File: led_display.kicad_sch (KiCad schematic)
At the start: 192 parts, among them J6 Conn_02x07_Odd_Even

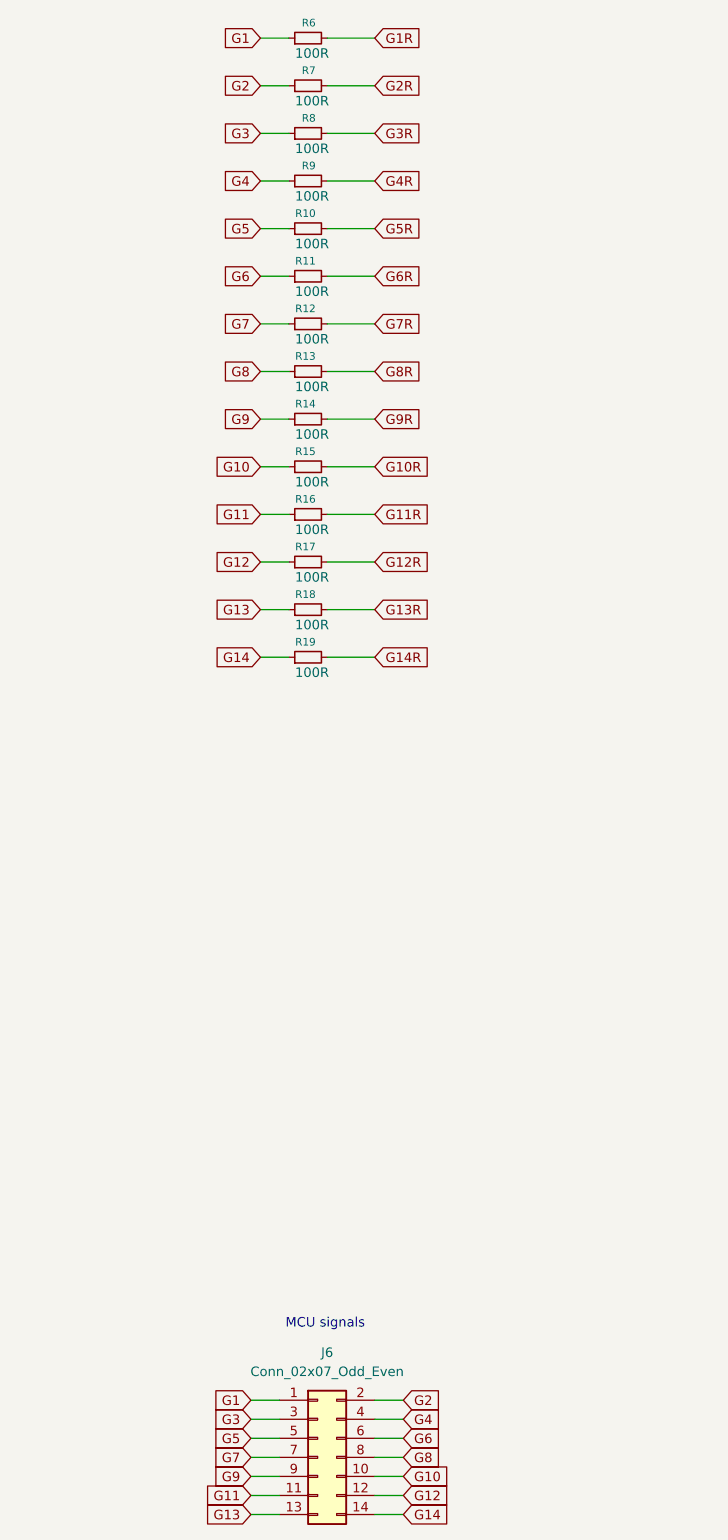
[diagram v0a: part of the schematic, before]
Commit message: Change of concept - one board, not multiple
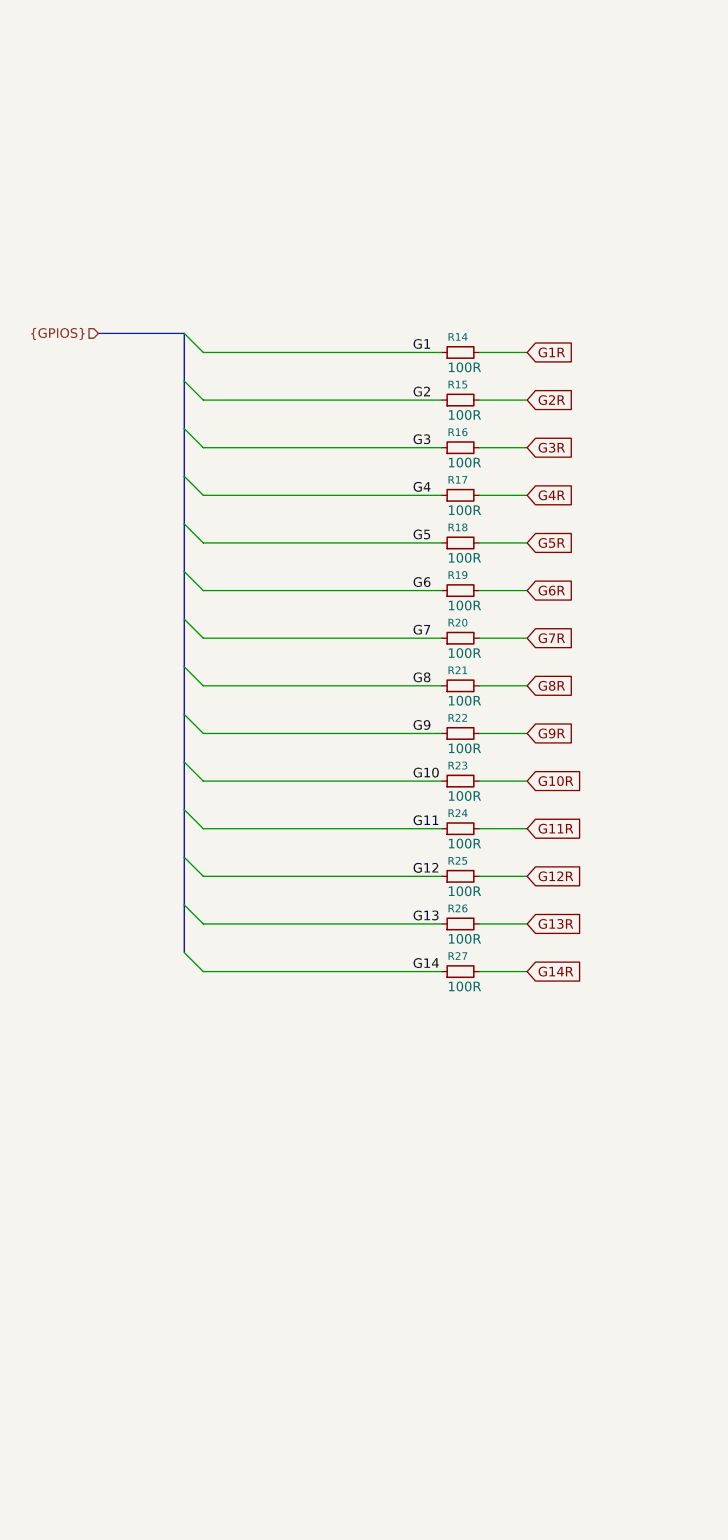
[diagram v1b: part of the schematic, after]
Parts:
- removed J6: Conn_02x07_Odd_Even, Connector_PinHeader_2.54mm:PinHeader_2x07_P2.54mm_Vertical, symbol Connector_Generic:Conn_02x07_Odd_Even
- renumbered R6 to R14, R7 to R15, R8 to R16, R9 to R17, R10 to R18, R11 to R19, R12 to R20, R13 to R21, R14 to R22, R15 to R23, R16 to R24, R17 to R25, R18 to R26, R19 to R27
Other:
- note removed: "MCU signals"
- moved on the sheet: R14, R15, R16, R17, R18, R19, R20, R21, R22, R23, R24, R25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

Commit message: Early pcb project
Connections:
- net G10R: now also D114.1 (K)
- net G11R: now also D115.1 (K)
- net G12R: now also D116.1 (K)
- net G13R: now also D117.1 (K)
- net G14R: now also D118.1 (K)
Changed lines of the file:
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@@
 	(global_label "G11R"
 		(shape input)
-		(at 232.41 153.67 270)
+		(at 233.68 153.67 270)
 		(fields_autoplaced yes)
 		(effects
@@
 		)
 		(property "Intersheetrefs" "${INTERSHEET_REFS}"
-			(at 232.41 161.6142 90)
+			(at 233.68 161.6142 90)
 			(effects
 				(font
@@
 	(global_label "G12R"
 		(shape input)
-		(at 245.11 153.67 270)
+		(at 246.38 153.67 270)
 		(fields_autoplaced yes)
 		(effects
@@
 		)
 		(property "Intersheetrefs" "${INTERSHEET_REFS}"
-			(at 245.11 161.6142 90)
+			(at 246.38 161.6142 90)
 			(effects
 				(font
@@
 	(global_label "G14R"
 		(shape input)
-		(at 270.51 153.67 270)
+		(at 271.78 153.67 270)
 		(fields_autoplaced yes)
 		(effects
@@
 		)
 		(property "Intersheetrefs" "${INTERSHEET_REFS}"
-			(at 270.51 161.6142 90)
+			(at 271.78 161.6142 90)
 			(effects
 				(font
@@
 	(global_label "G13R"
 		(shape input)
-		(at 257.81 153.67 270)
+		(at 259.08 153.67 270)
 		(fields_autoplaced yes)
 		(effects
@@
 		)
 		(property "Intersheetrefs" "${INTERSHEET_REFS}"
-			(at 257.81 161.6142 90)
+			(at 259.08 161.6142 90)
 			(effects
 				(font
@@
 	(global_label "G10R"
 		(shape input)
-		(at 219.71 153.67 270)
+		(at 220.98 153.67 270)
 		(fields_autoplaced yes)
 		(effects
@@
 		)
 		(property "Intersheetrefs" "${INTERSHEET_REFS}"
-			(at 219.71 161.6142 90)
+			(at 220.98 161.6142 90)
 			(effects
 				(font

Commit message: Finished pcb project
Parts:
- renumbered D69 to D10, D22 to D100, D34 to D101, D47 to D102, D61 to D103, D76 to D104, D91 to D105, D121 to D107, D135 to D108, D148 to D109, D84 to D11, D160 to D110, D170 to D111, D177 to D112, D6 to D113, D13 to D114, D23 to D115, D35 to D116, D48 to D117, D62 to D118, D77 to D119, D99 to D12, D92 to D120, D107 to D121, D136 to D123, D149 to D124, D161 to D125, D171 to D126, D178 to D127, D14 to D128, D24 to D129, D114 to D13, D36 to D130, D49 to D131, D63 to D132, D78 to D133, D93 to D134, D108 to D135, D123 to D136, D150 to D138, D162 to D139, D128 to D14, D172 to D140, D15 to D141, D25 to D142, D37 to D143, D50 to D144, D64 to D145, D79 to D146, D94 to D147, D109 to D148, D124 to D149, D141 to D15, D138 to D150, D163 to D152, D173 to D153, D26 to D154, D38 to D155, D51 to D156, D65 to D157, D80 to D158, D95 to D159, D110 to D160, D125 to D161, D139 to D162, D152 to D163, D39 to D165, D52 to D166, D66 to D167, D81 to D168, D96 to D169, D28 to D17, D111 to D170, D126 to D171, D140 to D172, D153 to D173, D67 to D174, D82 to D175, D97 to D176, D112 to D177, D127 to D178, D41 to D18, D55 to D19, D53 to D2, D70 to D20, D85 to D21, D100 to D22, D115 to D23, D129 to D24, D142 to D25, D154 to D26, D7 to D27, D17 to D28, D68 to D3, D42 to D30, D56 to D31, D71 to D32, D86 to D33, D101 to D34, D116 to D35, D130 to D36, D143 to D37, D155 to D38, D165 to D39, D83 to D4, D8 to D40, D18 to D41, D30 to D42, D57 to D44, D72 to D45, D87 to D46, D102 to D47, D117 to D48, D131 to D49, D98 to D5, D144 to D50, D156 to D51, D166 to D52, D2 to D53, D9 to D54, D19 to D55, D31 to D56, D44 to D57, D73 to D59, D113 to D6, D88 to D60, D103 to D61, D118 to D62, D132 to D63, D145 to D64, D157 to D65, D167 to D66, D174 to D67, D3 to D68, D10 to D69, D27 to D7, D20 to D70, D32 to D71, D45 to D72, D59 to D73, D89 to D75, D104 to D76, D119 to D77, D133 to D78, D146 to D79, D40 to D8, D158 to D80, D168 to D81, D175 to D82, D4 to D83, D11 to D84, D21 to D85, D33 to D86, D46 to D87, D60 to D88, D75 to D89, D54 to D9, D105 to D91, D120 to D92, D134 to D93, D147 to D94, D159 to D95, D169 to D96, D176 to D97, D5 to D98, D12 to D99, R17 to R10, R18 to R11, R19 to R12, R20 to R13, R21 to R14, R22 to R15, R23 to R16, R24 to R17, R25 to R18, R26 to R19, R27 to R20, R14 to R7, R15 to R8, R16 to R9
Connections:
- net G10R: now also D14.2 (A), D161.2 (A), D171.2 (A), D49.2 (A)

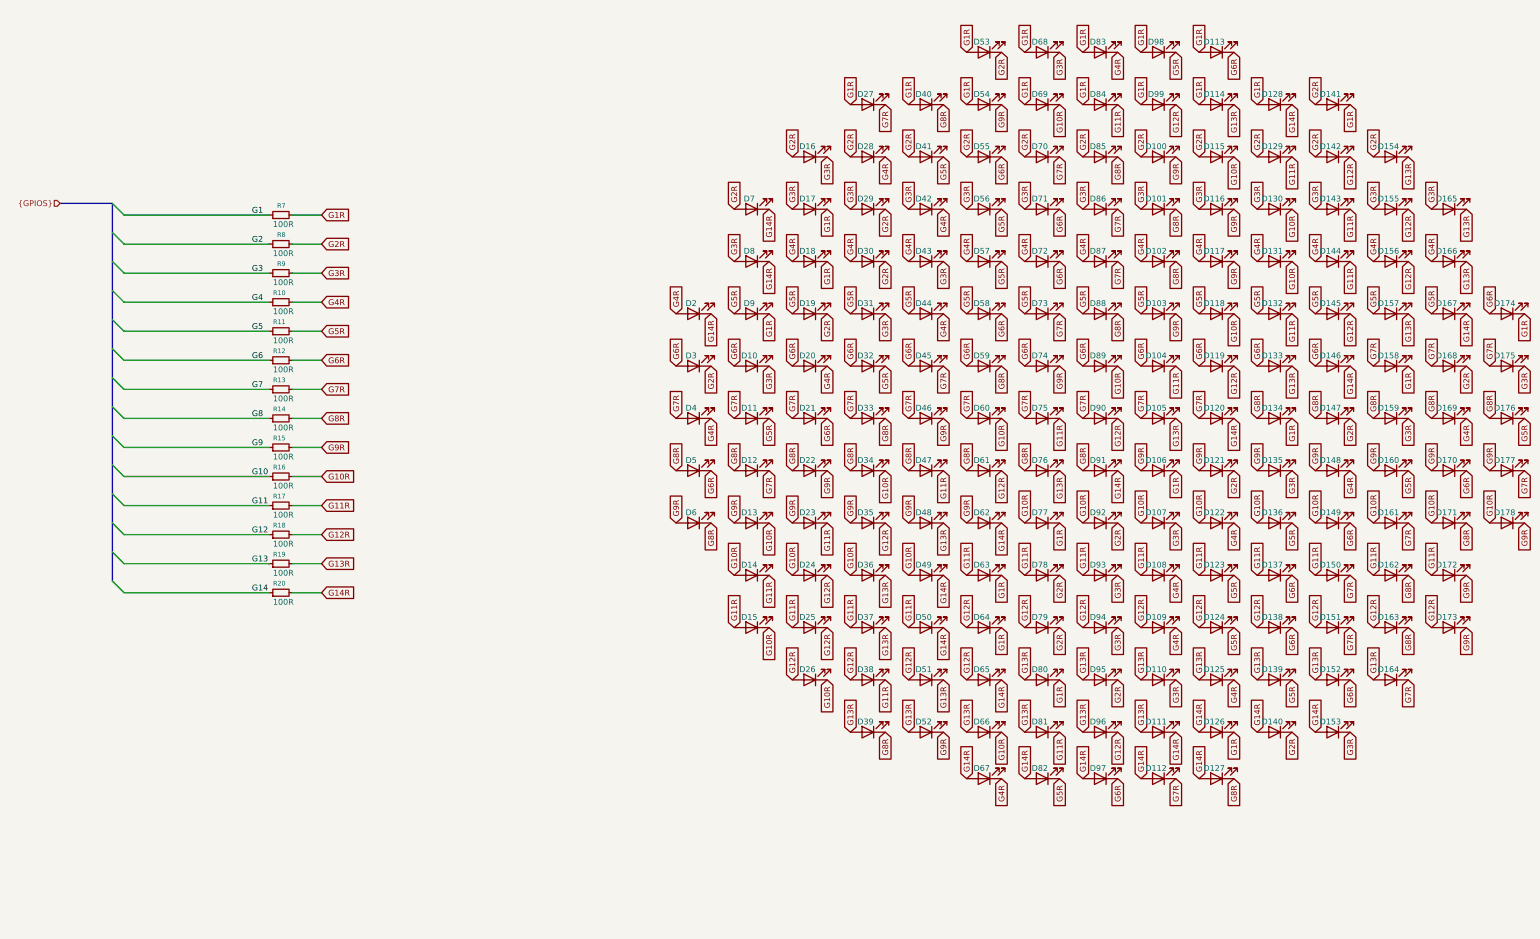
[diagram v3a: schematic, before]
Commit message: Add new mcu and better leds layout
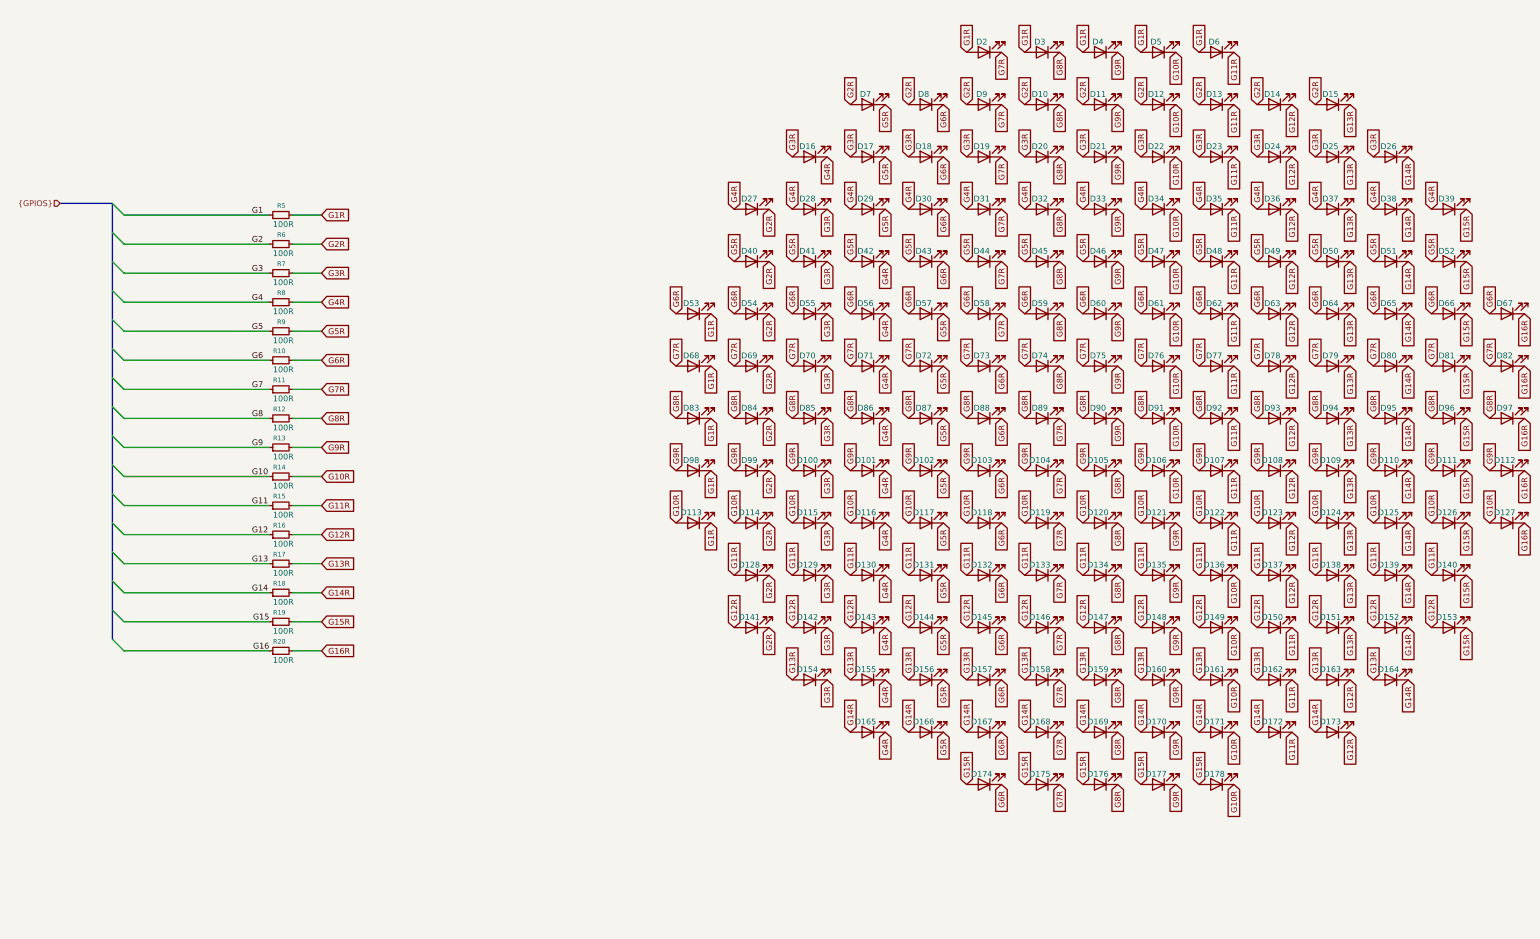
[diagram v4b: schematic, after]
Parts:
- added R19, R20: 100R, Resistor_SMD:R_0603_1608Metric, symbol Device:R_Small
- renumbered D69 to D10, D22 to D100, D34 to D101, D47 to D102, D61 to D103, D76 to D104, D91 to D105, D121 to D107, D135 to D108, D148 to D109, D84 to D11, D160 to D110, D170 to D111, D177 to D112, D6 to D113, D13 to D114, D23 to D115, D35 to D116, D48 to D117, D62 to D118, D77 to D119, D99 to D12, D92 to D120, D107 to D121, D136 to D123, D149 to D124, D161 to D125, D171 to D126, D178 to D127, D14 to D128, D24 to D129, D114 to D13, D36 to D130, D49 to D131, D63 to D132, D78 to D133, D93 to D134, D108 to D135, D123 to D136, D150 to D138, D162 to D139, D128 to D14, D172 to D140, D15 to D141, D25 to D142, D37 to D143, D50 to D144, D64 to D145, D79 to D146, D94 to D147, D109 to D148, D124 to D149, D141 to D15, D138 to D150, D163 to D152, D173 to D153, D26 to D154, D38 to D155, D51 to D156, D65 to D157, D80 to D158, D95 to D159, D110 to D160, D125 to D161, D139 to D162, D152 to D163, D39 to D165, D52 to D166, D66 to D167, D81 to D168, D96 to D169, D28 to D17, D111 to D170, D126 to D171, D140 to D172, D153 to D173, D67 to D174, D82 to D175, D97 to D176, D112 to D177, D127 to D178, D41 to D18, D55 to D19, D53 to D2, D70 to D20, D85 to D21, D100 to D22, D115 to D23, D129 to D24, D142 to D25, D154 to D26, D7 to D27, D17 to D28, D68 to D3, D42 to D30, D56 to D31, D71 to D32, D86 to D33, D101 to D34, D116 to D35, D130 to D36, D143 to D37, D155 to D38, D165 to D39, D83 to D4, D8 to D40, D18 to D41, D30 to D42, D57 to D44, D72 to D45, D87 to D46, D102 to D47, D117 to D48, D131 to D49, D98 to D5, D144 to D50, D156 to D51, D166 to D52, D2 to D53, D9 to D54, D19 to D55, D31 to D56, D44 to D57, D73 to D59, D113 to D6, D88 to D60, D103 to D61, D118 to D62, D132 to D63, D145 to D64, D157 to D65, D167 to D66, D174 to D67, D3 to D68, D10 to D69, D27 to D7, D20 to D70, D32 to D71, D45 to D72, D59 to D73, D89 to D75, D104 to D76, D119 to D77, D133 to D78, D146 to D79, D40 to D8, D158 to D80, D168 to D81, D175 to D82, D4 to D83, D11 to D84, D21 to D85, D33 to D86, D46 to D87, D60 to D88, D75 to D89, D54 to D9, D105 to D91, D120 to D92, D134 to D93, D147 to D94, D159 to D95, D169 to D96, D176 to D97, D5 to D98, D12 to D99, R12 to R10, R13 to R11, R14 to R12, R15 to R13, R16 to R14, R17 to R15, R18 to R16, R19 to R17, R20 to R18, R7 to R5, R8 to R6, R9 to R7, R10 to R8, R11 to R9
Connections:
- net G10R: now also D106.1 (K), D113.2 (A), D114.2 (A), D115.2 (A), D116.2 (A), D117.2 (A), D118.2 (A), D12.1 (K), D136.1 (K), D149.1 (K), D161.1 (K), D171.1 (K), D178.1 (K), D22.1 (K), D34.1 (K), D47.1 (K), D5.1 (K), D61.1 (K), D76.1 (K), D91.1 (K); no longer D10.1 (K), D101.1 (K), D114.1 (K), D128.2 (A), D129.2 (A), D130.2 (A), D131.2 (A), D141.1 (K), D154.1 (K), D167.1 (K), D23.1 (K), D36.1 (K), D49.1 (K), D62.1 (K), D75.1 (K), D88.1 (K)
- net G11R: now also D107.1 (K), D122.1 (K), D128.2 (A), D129.2 (A), D13.1 (K), D130.2 (A), D131.2 (A), D150.1 (K), D162.1 (K), D172.1 (K), D23.1 (K), D35.1 (K), D48.1 (K), D6.1 (K), D62.1 (K), D77.1 (K), D92.1 (K); no longer D102.1 (K), D11.1 (K), D115.1 (K), D128.1 (K), D141.2 (A), D142.2 (A), D143.2 (A), D144.2 (A), D155.1 (K), D168.1 (K), D24.1 (K), D37.1 (K), D50.1 (K), D63.1 (K), D76.1 (K), D89.1 (K)
- net G12R: now also D108.1 (K), D123.1 (K), D137.1 (K), D14.1 (K), D141.2 (A), D142.2 (A), D143.2 (A), D144.2 (A), D163.1 (K), D173.1 (K), D24.1 (K), D36.1 (K), D49.1 (K), D63.1 (K), D78.1 (K), D93.1 (K); no longer D103.1 (K), D116.1 (K), D12.1 (K), D129.1 (K), D142.1 (K), D154.2 (A), D155.2 (A), D156.2 (A), D157.2 (A), D169.1 (K), D25.1 (K), D38.1 (K), D51.1 (K), D64.1 (K), D77.1 (K), D90.1 (K)
- net G13R: now also D109.1 (K), D124.1 (K), D138.1 (K), D15.1 (K), D151.1 (K), D154.2 (A), D155.2 (A), D156.2 (A), D157.2 (A), D25.1 (K), D37.1 (K), D50.1 (K), D64.1 (K), D79.1 (K), D94.1 (K); no longer D104.1 (K), D117.1 (K), D13.1 (K), D130.1 (K), D143.1 (K), D156.1 (K), D165.2 (A), D166.2 (A), D167.2 (A), D168.2 (A), D169.2 (A), D170.2 (A), D26.1 (K), D39.1 (K), D52.1 (K), D65.1 (K), D78.1 (K), D91.1 (K)
- net G14R: now also D110.1 (K), D125.1 (K), D139.1 (K), D152.1 (K), D164.1 (K), D165.2 (A), D166.2 (A), D167.2 (A), D168.2 (A), D169.2 (A), D170.2 (A), D26.1 (K), D38.1 (K), D51.1 (K), D65.1 (K), D80.1 (K), D95.1 (K); no longer D105.1 (K), D118.1 (K), D131.1 (K), D14.1 (K), D144.1 (K), D157.1 (K), D170.1 (K), D174.2 (A), D175.2 (A), D176.2 (A), D177.2 (A), D178.2 (A), D27.1 (K), D40.1 (K), D53.1 (K), D66.1 (K), D79.1 (K), D92.1 (K)
- net G1R: now also D113.1 (K), D53.1 (K), D68.1 (K), D83.1 (K), D98.1 (K); no longer D10.2 (A), D106.1 (K), D11.2 (A), D119.1 (K), D12.2 (A), D13.2 (A), D132.1 (K), D14.2 (A), D145.1 (K), D15.1 (K), D158.1 (K), D171.1 (K), D28.1 (K), D41.1 (K), D54.1 (K), D67.1 (K), D7.2 (A), D8.2 (A), D80.1 (K), D9.2 (A), D93.1 (K)
- net G2R: now also D10.2 (A), D11.2 (A), D114.1 (K), D12.2 (A), D128.1 (K), D13.2 (A), D14.2 (A), D141.1 (K), D27.1 (K), D40.1 (K), D54.1 (K), D69.1 (K), D7.2 (A), D8.2 (A), D84.1 (K), D9.2 (A), D99.1 (K); no longer D107.1 (K), D120.1 (K), D133.1 (K), D146.1 (K), D159.1 (K), D16.2 (A), D17.2 (A), D172.1 (K), D18.2 (A), D19.2 (A), D2.1 (K), D20.2 (A), D21.2 (A), D22.2 (A), D23.2 (A), D24.2 (A), D25.2 (A), D26.2 (A), D27.2 (A), D29.1 (K), D42.1 (K), D55.1 (K), D68.1 (K), D81.1 (K), D94.1 (K)
- net G3R: now also D100.1 (K), D115.1 (K), D129.1 (K), D142.1 (K), D154.1 (K), D16.2 (A), D17.2 (A), D18.2 (A), D19.2 (A), D20.2 (A), D21.2 (A), D22.2 (A), D23.2 (A), D24.2 (A), D25.2 (A), D26.2 (A), D28.1 (K), D41.1 (K), D55.1 (K), D70.1 (K), D85.1 (K); no longer D108.1 (K), D121.1 (K), D134.1 (K), D147.1 (K), D16.1 (K), D160.1 (K), D173.1 (K), D28.2 (A), D29.2 (A), D3.1 (K), D30.2 (A), D31.2 (A), D32.2 (A), D33.2 (A), D34.2 (A), D35.2 (A), D36.2 (A), D37.2 (A), D38.2 (A), D39.2 (A), D40.2 (A), D43.1 (K), D56.1 (K), D69.1 (K), D82.1 (K), D95.1 (K)
- net G4R: now also D101.1 (K), D116.1 (K), D130.1 (K), D143.1 (K), D155.1 (K), D16.1 (K), D165.1 (K), D27.2 (A), D28.2 (A), D29.2 (A), D30.2 (A), D31.2 (A), D32.2 (A), D33.2 (A), D34.2 (A), D35.2 (A), D36.2 (A), D37.2 (A), D38.2 (A), D39.2 (A), D42.1 (K), D56.1 (K), D71.1 (K), D86.1 (K); no longer D109.1 (K), D122.1 (K), D135.1 (K), D148.1 (K), D161.1 (K), D17.1 (K), D174.1 (K), D30.1 (K), D4.1 (K), D41.2 (A), D42.2 (A), D43.2 (A), D44.2 (A), D45.2 (A), D46.2 (A), D47.2 (A), D48.2 (A), D49.2 (A), D50.2 (A), D51.2 (A), D52.2 (A), D53.2 (A), D57.1 (K), D70.1 (K), D83.1 (K), D96.1 (K)
- net G5R: now also D102.1 (K), D117.1 (K), D131.1 (K), D144.1 (K), D156.1 (K), D166.1 (K), D17.1 (K), D29.1 (K), D40.2 (A), D41.2 (A), D42.2 (A), D43.2 (A), D44.2 (A), D45.2 (A), D46.2 (A), D47.2 (A), D48.2 (A), D49.2 (A), D50.2 (A), D51.2 (A), D52.2 (A), D57.1 (K), D7.1 (K), D72.1 (K), D87.1 (K); no longer D110.1 (K), D123.1 (K), D136.1 (K), D149.1 (K), D162.1 (K), D175.1 (K), D18.1 (K), D31.1 (K), D44.1 (K), D5.1 (K), D54.2 (A), D55.2 (A), D56.2 (A), D57.2 (A), D58.2 (A), D59.2 (A), D60.2 (A), D61.2 (A), D62.2 (A), D63.2 (A), D64.2 (A), D65.2 (A), D66.2 (A), D71.1 (K), D84.1 (K), D97.1 (K)
- net G6R: now also D103.1 (K), D118.1 (K), D132.1 (K), D145.1 (K), D157.1 (K), D167.1 (K), D174.1 (K), D18.1 (K), D30.1 (K), D43.1 (K), D53.2 (A), D54.2 (A), D55.2 (A), D56.2 (A), D57.2 (A), D58.2 (A), D59.2 (A), D60.2 (A), D61.2 (A), D62.2 (A), D63.2 (A), D64.2 (A), D65.2 (A), D66.2 (A), D73.1 (K), D8.1 (K), D88.1 (K); no longer D111.1 (K), D124.1 (K), D137.1 (K), D150.1 (K), D163.1 (K), D176.1 (K), D19.1 (K), D32.1 (K), D45.1 (K), D58.1 (K), D6.1 (K), D68.2 (A), D69.2 (A), D70.2 (A), D71.2 (A), D72.2 (A), D73.2 (A), D74.2 (A), D75.2 (A), D76.2 (A), D77.2 (A), D78.2 (A), D79.2 (A), D85.1 (K), D98.1 (K)
- net G7R: now also D104.1 (K), D119.1 (K), D133.1 (K), D146.1 (K), D158.1 (K), D168.1 (K), D175.1 (K), D19.1 (K), D2.1 (K), D31.1 (K), D44.1 (K), D58.1 (K), D68.2 (A), D69.2 (A), D70.2 (A), D71.2 (A), D72.2 (A), D73.2 (A), D74.2 (A), D75.2 (A), D76.2 (A), D77.2 (A), D78.2 (A), D79.2 (A), D89.1 (K), D9.1 (K); no longer D112.1 (K), D125.1 (K), D138.1 (K), D151.1 (K), D164.1 (K), D177.1 (K), D20.1 (K), D33.1 (K), D46.1 (K), D59.1 (K), D7.1 (K), D72.1 (K), D83.2 (A), D84.2 (A), D85.2 (A), D86.2 (A), D87.2 (A), D88.2 (A), D89.2 (A), D90.2 (A), D91.2 (A), D92.2 (A), D99.1 (K)
- net G8R: now also D10.1 (K), D105.1 (K), D120.1 (K), D134.1 (K), D147.1 (K), D159.1 (K), D169.1 (K), D176.1 (K), D20.1 (K), D3.1 (K), D32.1 (K), D45.1 (K), D59.1 (K), D74.1 (K), D83.2 (A), D84.2 (A), D85.2 (A), D86.2 (A), D87.2 (A), D88.2 (A), D89.2 (A), D90.2 (A), D91.2 (A), D92.2 (A); no longer D100.2 (A), D101.2 (A), D102.2 (A), D103.2 (A), D104.2 (A), D105.2 (A), D113.1 (K), D126.1 (K), D139.1 (K), D152.1 (K), D165.1 (K), D178.1 (K), D21.1 (K), D34.1 (K), D47.1 (K), D60.1 (K), D73.1 (K), D8.1 (K), D86.1 (K), D98.2 (A), D99.2 (A)
- net G9R: now also D100.2 (A), D101.2 (A), D102.2 (A), D103.2 (A), D104.2 (A), D105.2 (A), D11.1 (K), D121.1 (K), D135.1 (K), D148.1 (K), D160.1 (K), D170.1 (K), D177.1 (K), D21.1 (K), D33.1 (K), D4.1 (K), D46.1 (K), D60.1 (K), D75.1 (K), D90.1 (K), D98.2 (A), D99.2 (A); no longer D100.1 (K), D113.2 (A), D114.2 (A), D115.2 (A), D116.2 (A), D117.2 (A), D118.2 (A), D127.1 (K), D140.1 (K), D153.1 (K), D166.1 (K), D22.1 (K), D35.1 (K), D48.1 (K), D61.1 (K), D74.1 (K), D87.1 (K), D9.1 (K)
- new net G15: R19.1
- new net G15R: D111.1 (K), D126.1 (K), D140.1 (K), D153.1 (K), D174.2 (A), D175.2 (A), D176.2 (A), D177.2 (A), D178.2 (A), D39.1 (K), D52.1 (K), D66.1 (K), D81.1 (K), D96.1 (K), R19.2
- new net G16: R20.1
- new net G16R: D112.1 (K), D127.1 (K), D67.1 (K), D82.1 (K), D97.1 (K), R20.2
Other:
- moved on the sheet: D174, D175, D176, D177, D178
